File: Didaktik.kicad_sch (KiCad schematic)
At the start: 102 parts, among them J1 USB_C_Receptacle_USB2.0, SW1 SW_Push, SW10 SW_Push_45deg, SW11 SW_Push_45deg, SW12 SW_Push_45deg, SW13 SW_Push_45deg, SW14 SW_Push_45deg, SW15 SW_Push_45deg, SW16 SW_Push_45deg, SW17 SW_Push_45deg, SW18 SW_Push_45deg, SW19 SW_Push_45deg, SW2 SW_Push_45deg, SW20 SW_Push_45deg, SW21 SW_Push_45deg, SW22 SW_Push_45deg, SW23 SW_Push_45deg, SW24 SW_Push_45deg, SW25 SW_Push_45deg, SW26 SW_Push_45deg, SW27 SW_Push_45deg, SW28 SW_Push_45deg, SW29 SW_Push_45deg, SW3 SW_Push_45deg, SW30 SW_Push_45deg, SW31 SW_Push_45deg, SW32 SW_Push_45deg, SW33 SW_Push_45deg, SW34 SW_Push_45deg, SW35 SW_Push_45deg, SW36 SW_Push_45deg, SW37 SW_Push_45deg, SW38 SW_Push_45deg, SW39 SW_Push_45deg, SW4 SW_Push_45deg, SW40 SW_Push_45deg, SW41 SW_Push_45deg, SW5 SW_Push_45deg, SW6 SW_Push_45deg, SW7 SW_Push_45deg, SW8 SW_Push_45deg, SW9 SW_Push_45deg, U1 ATmega32U4-M, Y1 Crystal_GND24_Small

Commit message: switch placement done, basic matrix routing done
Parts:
- D1, D10, D11, D12, D13, D14, D15, D16, D17, D18, D19, D2, D20, D21, D22, D23, D24, D26, D27, D28, D29, D3, D30, D31, D32, D33, D34, D35, D36, D37, D38, D39, D4, D40, D41, D5, D6, D7, D8, D9: footprint combodiode:ComboDiode -> Diode_SMD:D_SOD-123

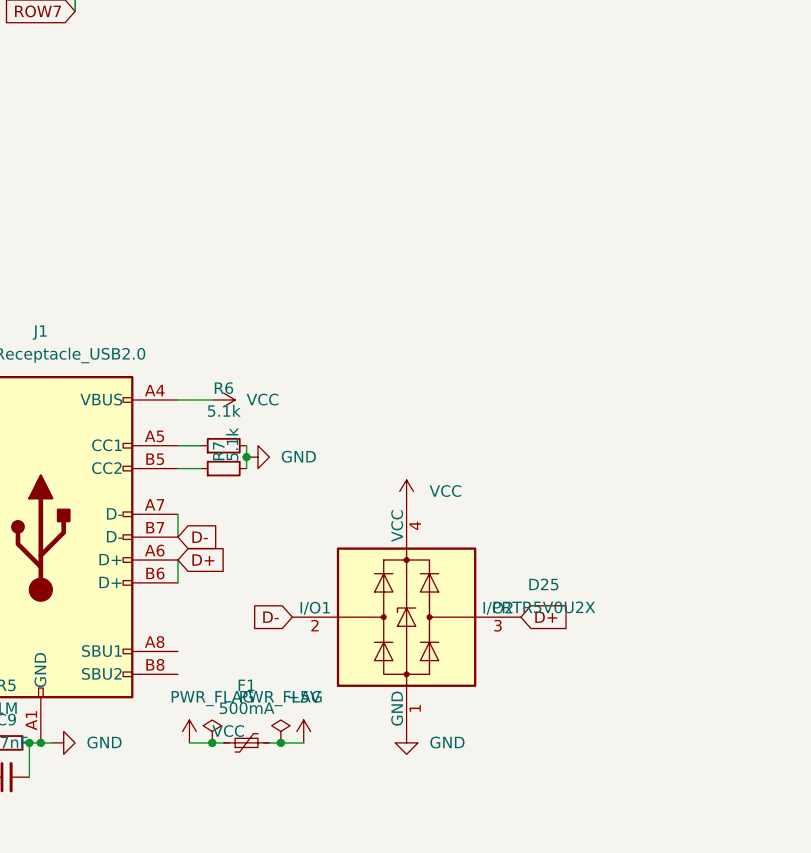
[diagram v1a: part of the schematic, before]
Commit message: added jts, started to arrange MCU components
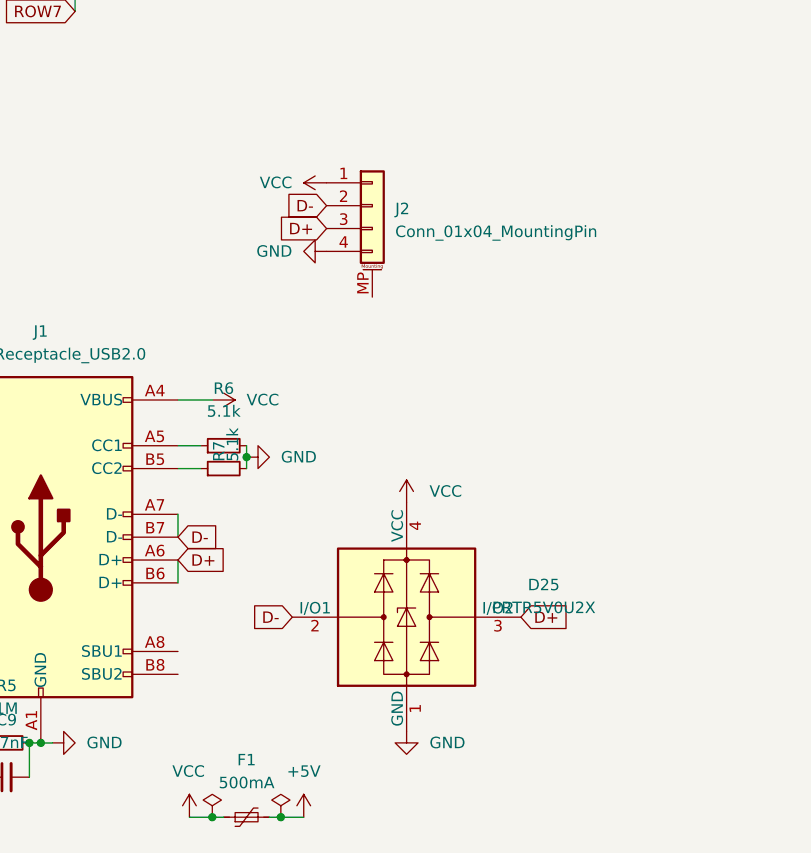
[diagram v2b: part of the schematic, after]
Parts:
- added J2: Conn_01x04_MountingPin, random-keyboard-parts:JST-SR-4, symbol Connector_Generic_MountingPin:Conn_01x04_MountingPin
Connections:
- net D+: now also J2.3 (Pin_3)
- net D-: now also J2.2 (Pin_2)
- net GND: now also J2.4 (Pin_4)
- net VCC: now also J2.1 (Pin_1)
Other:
- moved on the sheet: F1
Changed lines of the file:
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@@
 (kicad_sch (version 20211123) (generator eeschema)
   (paper "A4")
-  (junction (at 120.65 181.61) (diameter 0) (color 0 0 0 0)
+  (junction (at 120.65 189.865) (diameter 0) (color 0 0 0 0)
   )
   (junction (at 20.32 163.83) (diameter 0) (color 0 0 0 0)
@@
   (junction (at 153.67 56.515) (diameter 0) (color 0 0 0 0)
   )
-  (junction (at 128.27 181.61) (diameter 0) (color 0 0 0 0)
+  (junction (at 128.27 189.865) (diameter 0) (color 0 0 0 0)
   )
   (junction (at 133.35 73.025) (diameter 0) (color 0 0 0 0)
@@
     (stroke (width 0) (type default) (color 0 0 0 0))
   )
-  (wire (pts (xy 127 181.61) (xy 128.27 181.61))
+  (wire (pts (xy 127 189.865) (xy 128.27 189.865))
     (stroke (width 0) (type default) (color 0 0 0 0))
   )
@@
     (stroke (width 0) (type default) (color 0 0 0 0))
   )
-  (wire (pts (xy 120.65 181.61) (xy 121.92 181.61))
+  (wire (pts (xy 120.65 189.865) (xy 121.92 189.865))
     (stroke (width 0) (type default) (color 0 0 0 0))
   )
@@
     (stroke (width 0) (type default) (color 0 0 0 0))
   )
-  (wire (pts (xy 118.11 181.61) (xy 120.65 181.61))
+  (wire (pts (xy 118.11 189.865) (xy 120.65 189.865))
     (stroke (width 0) (type default) (color 0 0 0 0))
   )
@@
     (stroke (width 0) (type default) (color 0 0 0 0))
   )
-  (wire (pts (xy 128.27 181.61) (xy 130.81 181.61))
+  (wire (pts (xy 128.27 189.865) (xy 130.81 189.865))
     (stroke (width 0) (type default) (color 0 0 0 0))
   )
@@
     )
   )
+  (global_label "D+" (shape input) (at 133.35 124.46 180) (fields_autoplaced)
+    (effects (font (size 1.27 1.27)) (justify right))
+    (property "Intersheet References" "${INTERSHEET_REFS}" (id 0) (at 128.0945 124.5394 0)
+      (effects (font (size 1.27 1.27)) (justify right) hide)
+    )
+  )
+  (global_label "D-" (shape input) (at 133.35 121.92 180) (fields_autoplaced)
+    (effects (font (size 1.27 1.27)) (justify right))
+    (property "Intersheet References" "${INTERSHEET_REFS}" (id 0) (at 128.0945 121.9994 0)
+      (effects (font (size 1.27 1.27)) (justify right) hide)
+    )
+  )
   (global_label "COL0" (shape input) (at 120.65 38.1 90) (fields_autoplaced)
     (effects (font (size 1.27 1.27)) (justify left))
@@
     (pin "4")
   )
-  (symbol (lib_id "power:+5V") (at 130.81 181.61 0) (unit 1)
+  (symbol (lib_id "power:+5V") (at 130.81 189.865 0) (unit 1)
     (in_bom yes) (on_board yes) (fields_autoplaced)
-    (property "Reference" "#PWR0103" (id 0) (at 130.81 185.42 0)
+    (property "Reference" "#PWR0103" (id 0) (at 130.81 193.675 0)
       (effects (font (size 1.27 1.27)) hide)
     )
-    (property "Value" "+5V" (id 1) (at 130.81 176.53 0))
-    (property "Footprint" "" (id 2) (at 130.81 181.61 0)
+    (property "Value" "+5V" (id 1) (at 130.81 184.785 0))
+    (property "Footprint" "" (id 2) (at 130.81 189.865 0)
       (effects (font (size 1.27 1.27)) hide)
     )
-    (property "Datasheet" "" (id 3) (at 130.81 181.61 0)
+    (property "Datasheet" "" (id 3) (at 130.81 189.865 0)
       (effects (font (size 1.27 1.27)) hide)
     )
@@
     (pin "2")
   )
+  (symbol (lib_id "power:GND") (at 133.35 127 270) (unit 1)
+    (in_bom yes) (on_board yes) (fields_autoplaced)
+    (property "Reference" "#PWR0118" (id 0) (at 127 127 0)
+      (effects (font (size 1.27 1.27)) hide)
+    )
+    (property "Value" "GND" (id 1) (at 129.54 126.9999 90)
+      (effects (font (size 1.27 1.27)) (justify right))
+    )
+    (property "Footprint" "" (id 2) (at 133.35 127 0)
+      (effects (font (size 1.27 1.27)) hide)
+    )
+    (property "Datasheet" "" (id 3) (at 133.35 127 0)
+      (effects (font (size 1.27 1.27)) hide)
+    )
+    (pin "1")
+  )
   (symbol (lib_id "ComboDiode:D_Small") (at 115.57 80.645 270) (mirror x) (unit 1)
     (in_bom yes) (on_board yes)
@@
     (pin "2")
   )
-  (symbol (lib_id "ComboDiode:Polyfuse_Small") (at 124.46 181.61 90) (unit 1)
+  (symbol (lib_id "ComboDiode:Polyfuse_Small") (at 124.46 189.865 90) (unit 1)
     (in_bom yes) (on_board yes) (fields_autoplaced)
-    (property "Reference" "F1" (id 0) (at 124.46 175.26 90))
-    (property "Value" "500mA" (id 1) (at 124.46 177.8 90))
-    (property "Footprint" "Fuse:Fuse_1206_3216Metric" (id 2) (at 129.54 180.34 0)
+    (property "Reference" "F1" (id 0) (at 124.46 183.515 90))
+    (property "Value" "500mA" (id 1) (at 124.46 186.055 90))
+    (property "Footprint" "Fuse:Fuse_1206_3216Metric" (id 2) (at 129.54 188.595 0)
       (effects (font (size 1.27 1.27)) (justify left) hide)
     )
-    (property "Datasheet" "" (id 3) (at 124.46 181.61 0)
+    (property "Datasheet" "" (id 3) (at 124.46 189.865 0)
       (effects (font (size 1.27 1.27)) hide)
     )
@@
     (pin "2")
   )
+  (symbol (lib_id "Connector_Generic_MountingPin:Conn_01x04_MountingPin") (at 138.43 121.92 0) (unit 1)
+    (in_bom yes) (on_board yes) (fields_autoplaced)
+    (property "Reference" "J2" (id 0) (at 140.97 122.2755 0)
+      (effects (font (size 1.27 1.27)) (justify left))
+    )
+    (property "Value" "Conn_01x04_MountingPin" (id 1) (at 140.97 124.8155 0)
+      (effects (font (size 1.27 1.27)) (justify left))
+    )
+    (property "Footprint" "random-keyboard-parts:JST-SR-4" (id 2) (at 138.43 121.92 0)
+      (effects (font (size 1.27 1.27)) hide)
+    )
+    (property "Datasheet" "~" (id 3) (at 138.43 121.92 0)
+      (effects (font (size 1.27 1.27)) hide)
+    )
+    (pin "1")
+    (pin "2")
+    (pin "3")
+    (pin "4")
+    (pin "MP")
+  )
   (symbol (lib_id "Connector:USB_C_Receptacle_USB2.0") (at 101.6 158.75 0) (unit 1)
     (in_bom yes) (on_board yes) (fields_autoplaced)
@@
     (pin "2")
   )
-  (symbol (lib_id "power:PWR_FLAG") (at 128.27 181.61 0) (unit 1)
+  (symbol (lib_id "power:PWR_FLAG") (at 128.27 189.865 0) (unit 1)
     (in_bom yes) (on_board yes) (fields_autoplaced)
-    (property "Reference" "#FLG0101" (id 0) (at 128.27 179.705 0)
+    (property "Reference" "#FLG0101" (id 0) (at 128.27 187.96 0)
       (effects (font (size 1.27 1.27)) hide)
     )
-    (property "Value" "PWR_FLAG" (id 1) (at 128.27 176.53 0))
-    (property "Footprint" "" (id 2) (at 128.27 181.61 0)
+    (property "Value" "PWR_FLAG" (id 1) (at 128.27 184.785 0)
       (effects (font (size 1.27 1.27)) hide)
     )
-    (property "Datasheet" "~" (id 3) (at 128.27 181.61 0)
+    (property "Footprint" "" (id 2) (at 128.27 189.865 0)
+      (effects (font (size 1.27 1.27)) hide)
+    )
+    (property "Datasheet" "~" (id 3) (at 128.27 189.865 0)
       (effects (font (size 1.27 1.27)) hide)
     )
@@
     (pin "1")
   )
-  (symbol (lib_id "power:VCC") (at 118.11 181.61 0) (unit 1)
-    (in_bom yes) (on_board yes) (fields_autoplaced)
-    (property "Reference" "#PWR0114" (id 0) (at 118.11 185.42 0)
+  (symbol (lib_id "power:VCC") (at 118.11 189.865 0) (unit 1)
+    (in_bom yes) (on_board yes)
+    (property "Reference" "#PWR0114" (id 0) (at 118.11 193.675 0)
       (effects (font (size 1.27 1.27)) hide)
     )
-    (property "Value" "VCC" (id 1) (at 120.65 180.3399 0)
+    (property "Value" "VCC" (id 1) (at 116.205 184.785 0)
       (effects (font (size 1.27 1.27)) (justify left))
     )
-    (property "Footprint" "" (id 2) (at 118.11 181.61 0)
+    (property "Footprint" "" (id 2) (at 118.11 189.865 0)
       (effects (font (size 1.27 1.27)) hide)
     )
-    (property "Datasheet" "" (id 3) (at 118.11 181.61 0)
+    (property "Datasheet" "" (id 3) (at 118.11 189.865 0)
       (effects (font (size 1.27 1.27)) hide)
     )
@@
     (pin "2")
   )
-  (symbol (lib_id "power:PWR_FLAG") (at 120.65 181.61 0) (unit 1)
+  (symbol (lib_id "power:PWR_FLAG") (at 120.65 189.865 0) (unit 1)
     (in_bom yes) (on_board yes) (fields_autoplaced)
-    (property "Reference" "#FLG0102" (id 0) (at 120.65 179.705 0)
+    (property "Reference" "#FLG0102" (id 0) (at 120.65 187.96 0)
       (effects (font (size 1.27 1.27)) hide)
     )
-    (property "Value" "PWR_FLAG" (id 1) (at 120.65 176.53 0))
-    (property "Footprint" "" (id 2) (at 120.65 181.61 0)
+    (property "Value" "PWR_FLAG" (id 1) (at 120.65 184.785 0)
       (effects (font (size 1.27 1.27)) hide)
     )
-    (property "Datasheet" "~" (id 3) (at 120.65 181.61 0)
+    (property "Footprint" "" (id 2) (at 120.65 189.865 0)
+      (effects (font (size 1.27 1.27)) hide)
+    )
+    (property "Datasheet" "~" (id 3) (at 120.65 189.865 0)
       (effects (font (size 1.27 1.27)) hide)
     )
@@
     (pin "4")
   )
+  (symbol (lib_id "power:VCC") (at 133.35 119.38 90) (unit 1)
+    (in_bom yes) (on_board yes) (fields_autoplaced)
+    (property "Reference" "#PWR0119" (id 0) (at 137.16 119.38 0)
+      (effects (font (size 1.27 1.27)) hide)
+    )
+    (property "Value" "VCC" (id 1) (at 129.54 119.3799 90)
+      (effects (font (size 1.27 1.27)) (justify left))
+    )
+    (property "Footprint" "" (id 2) (at 133.35 119.38 0)
+      (effects (font (size 1.27 1.27)) hide)
+    )
+    (property "Datasheet" "" (id 3) (at 133.35 119.38 0)
+      (effects (font (size 1.27 1.27)) hide)
+    )
+    (pin "1")
+  )
   (symbol (lib_id "Switch:SW_Push_45deg") (at 168.91 62.865 0) (mirror y) (unit 1)
     (in_bom yes) (on_board yes)
@@
       (reference "#PWR0117") (unit 1) (value "+5V") (footprint "")
     )
+    (path "/1125cca0-df7f-4a88-bbd1-82157158d6af"
+      (reference "#PWR0118") (unit 1) (value "GND") (footprint "")
+    )
+    (path "/eb66535e-aede-4639-9194-854f18e0560a"
+      (reference "#PWR0119") (unit 1) (value "VCC") (footprint "")
+    )
     (path "/4288a19a-13d9-4091-890e-2cc91277147e"
       (reference "C1") (unit 1) (value "0.1uF") (footprint "Capacitor_SMD:C_0402_1005Metric")
@@
       (reference "J1") (unit 1) (value "USB_C_Receptacle_USB2.0") (footprint "Connector_USB:USB_C_Receptacle_HRO_TYPE-C-31-M-12")
     )
+    (path "/773ca0f3-ad89-40fc-bb52-d706b4c154be"
+      (reference "J2") (unit 1) (value "Conn_01x04_MountingPin") (footprint "random-keyboard-parts:JST-SR-4")
+    )
     (path "/1b233532-9656-4e4e-a0b7-8260db2f2d5f"

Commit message: added leds
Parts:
- added C10, C11: C_Small, Capacitor_SMD:C_0402_1005Metric, symbol ComboDiode:C_Small
- added D42: LED, symbol ComboDiode:LED
- added D43: LED, Keebio-Parts:LED_3mm, symbol ComboDiode:LED
- added R8, R9: R_Small, Resistor_SMD:R_0402_1005Metric, symbol ComboDiode:R_Small
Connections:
- net GND: now also D42.1 (K), D43.1 (K)
- new net: D43.2 (A), R9.2
- new net: D42.2 (A), R8.2
- new net LED Power: R8.1
- new net LED capslock: R9.1

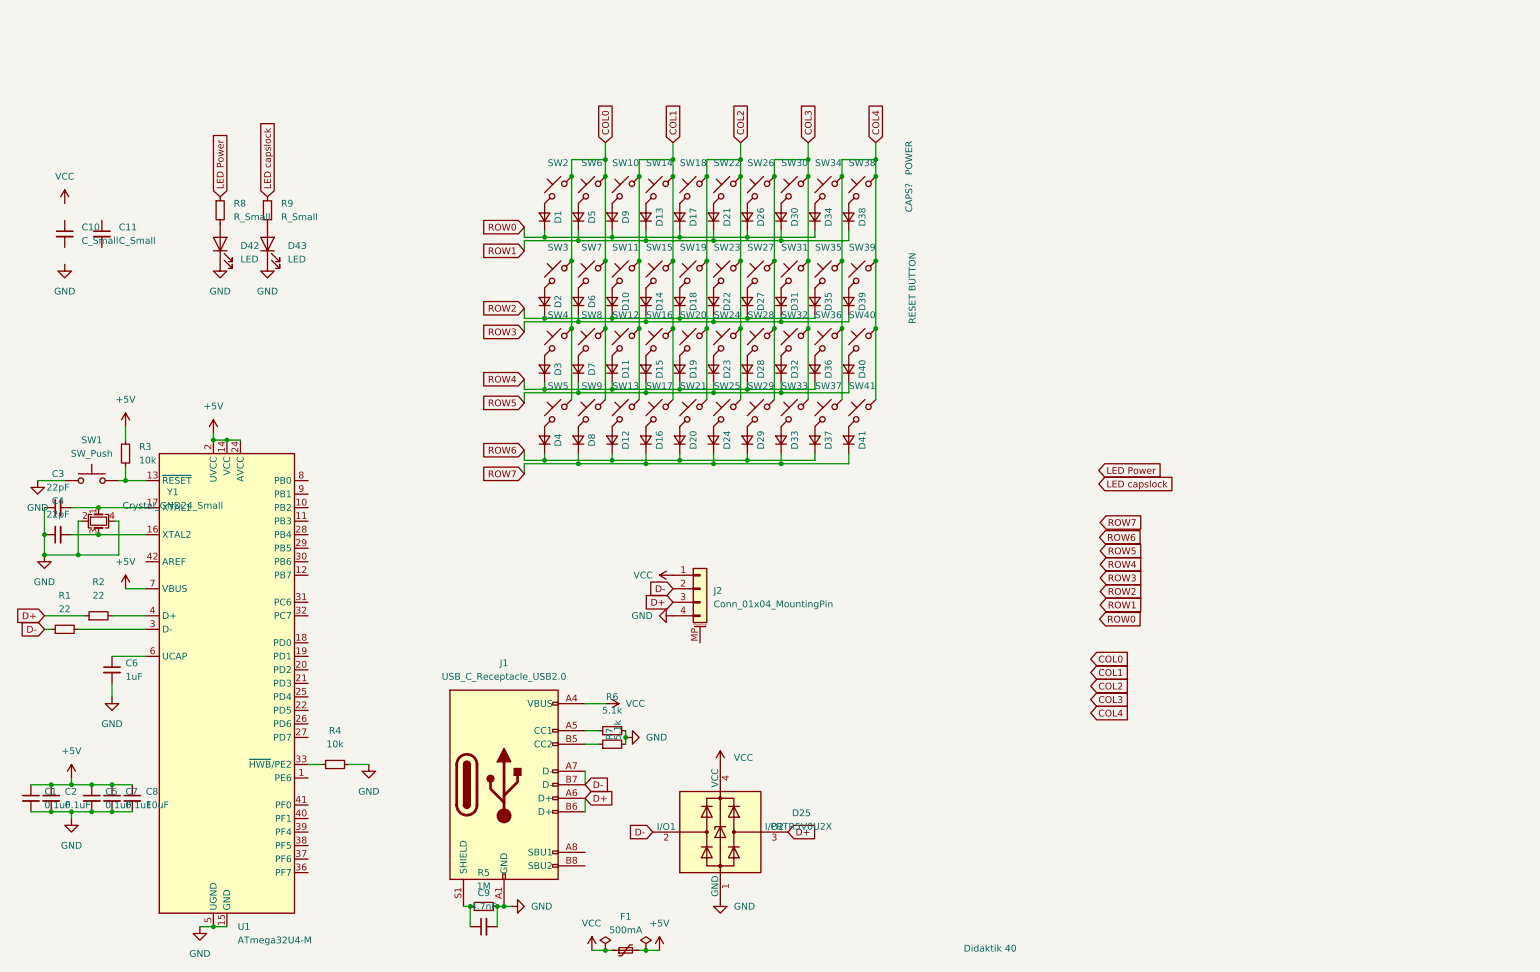
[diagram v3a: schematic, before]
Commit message: cleaned schematics, continued routing
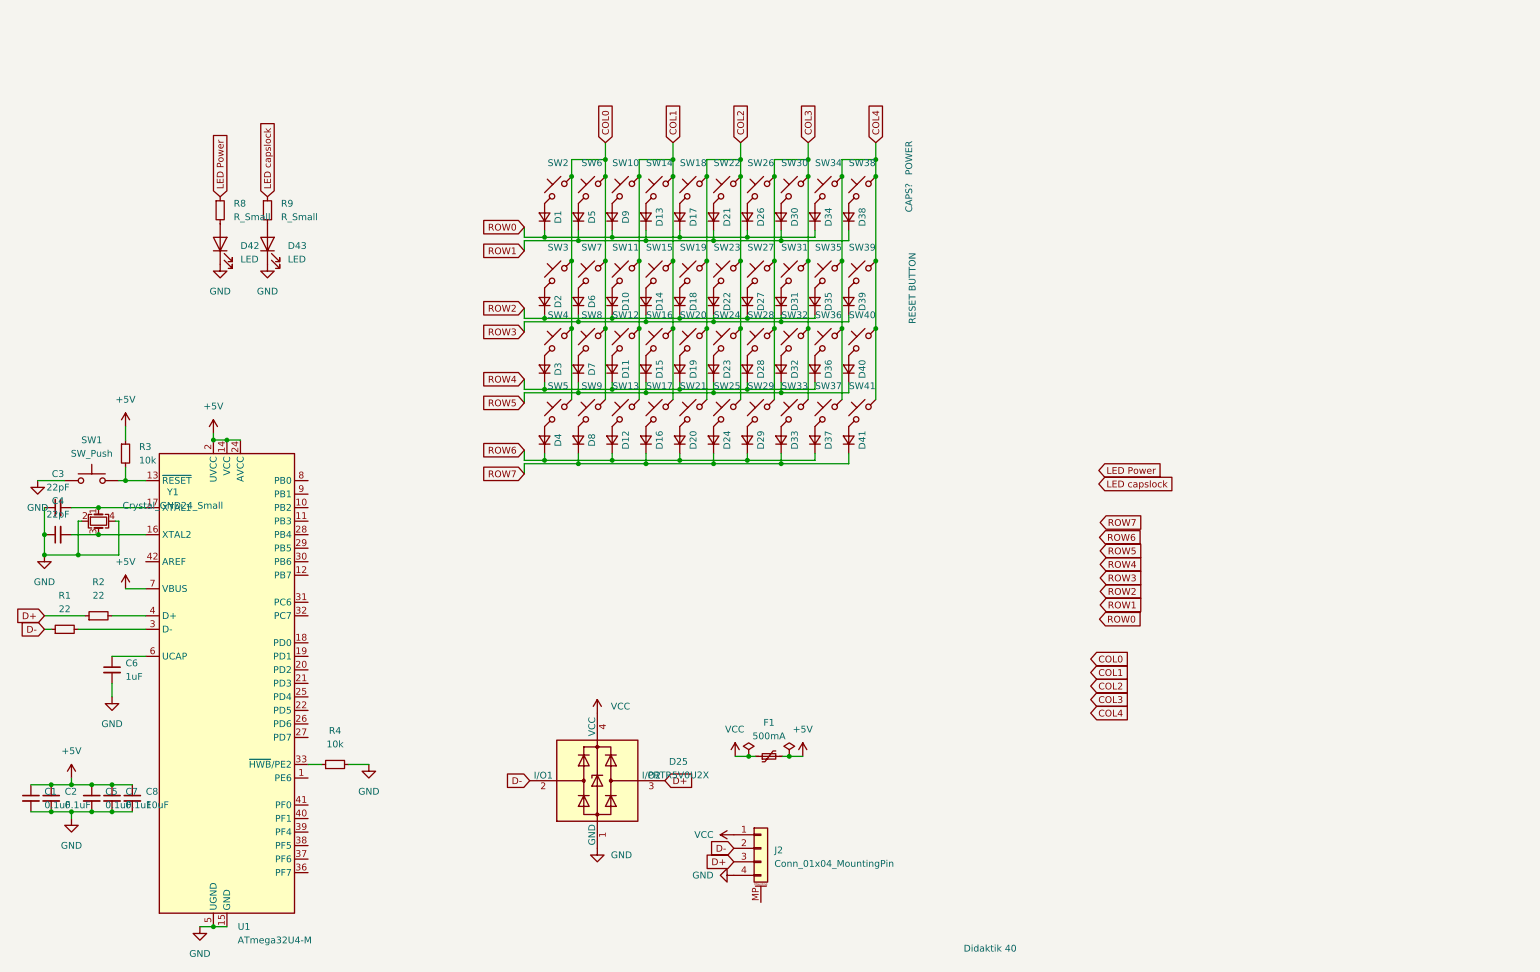
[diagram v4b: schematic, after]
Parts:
- removed C10, C11: C_Small, Capacitor_SMD:C_0402_1005Metric, symbol ComboDiode:C_Small
- removed C9: 4.7nF, Capacitor_SMD:C_0402_1005Metric, symbol ComboDiode:C_Small
- removed J1: USB_C_Receptacle_USB2.0, Connector_USB:USB_C_Receptacle_HRO_TYPE-C-31-M-12, symbol Connector:USB_C_Receptacle_USB2.0
- removed R5: 1M, Resistor_SMD:R_0402_1005Metric, symbol ComboDiode:R_Small
- removed R6, R7: 5.1k, Resistor_SMD:R_0402_1005Metric, symbol ComboDiode:R_Small
- D42: footprint (none) -> Keebio-Parts:LED_3mm
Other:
- moved on the sheet: D25, F1, J2
